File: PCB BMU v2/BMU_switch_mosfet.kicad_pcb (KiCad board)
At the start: 2 copper layers, 18 parts, among them Q1 BC337, Q10 IRF4905STRLPBF, Q2 IRF4905STRLPBF, Q3 IRF4905STRLPBF, Q4 IRF4905STRLPBF, Q5 IRF4905STRLPBF, Q6 BC337, Q7 IRF4905STRLPBF, Q8 IRF4905STRLPBF, Q9 IRF4905STRLPBF, U1 HX PZ2.54-1X2P ZZ, U2 ZX-IDC2.54-2-5PZZ, U3 ZX-IDC2.54-2-5PZZ

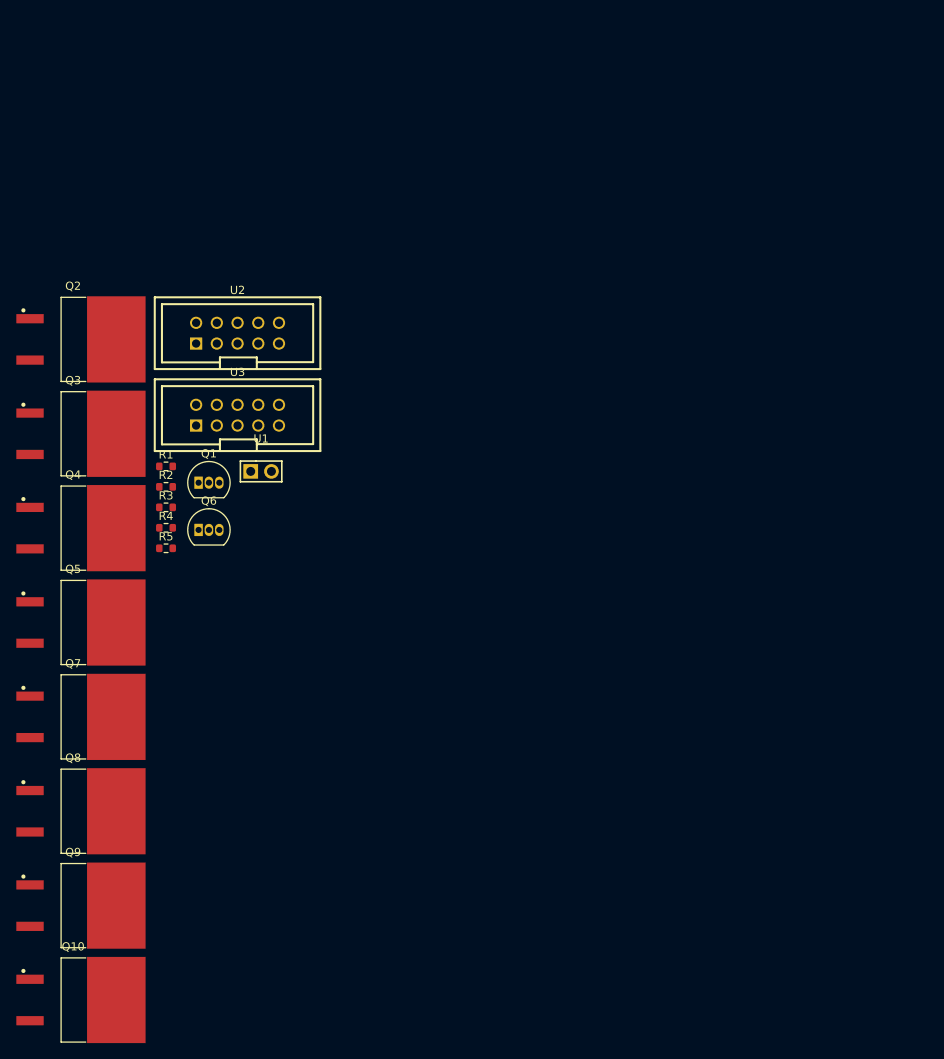
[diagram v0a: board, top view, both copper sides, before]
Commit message: add Ampère/Houre calculation
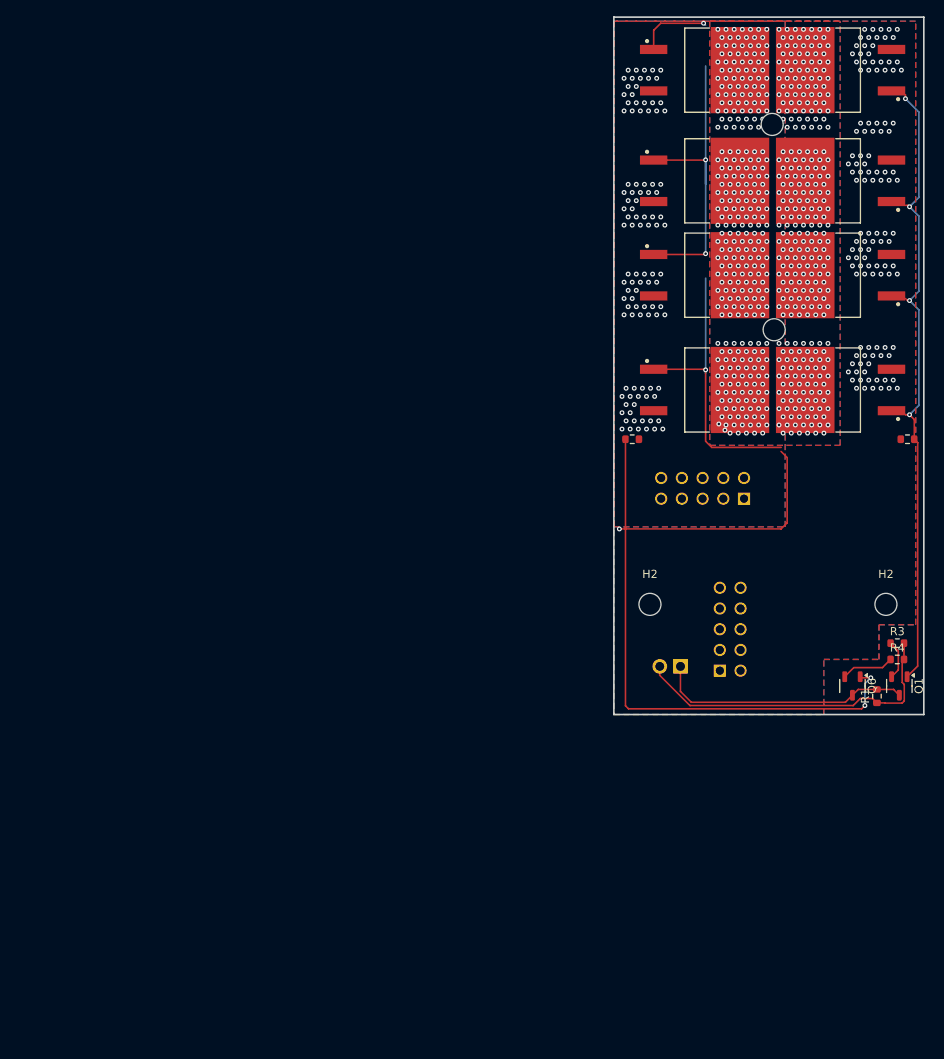
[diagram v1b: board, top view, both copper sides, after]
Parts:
- added H1: MountingHole, MountingHole:MountingHole_2.7mm_M2.5, B.Cu at (144.7, 49.8)
- added H1: MountingHole, MountingHole:MountingHole_2.7mm_M2.5, B.Cu at (144.4, 24.7)
- added H2: MountingHole, MountingHole:MountingHole_2.7mm_M2.5, F.Cu at (129.4, 83.5)
- added H2: MountingHole, MountingHole:MountingHole_2.7mm_M2.5, F.Cu at (158.4, 83.5)
- Q1, Q6: footprint Package_TO_SOT_THT:TO-92_Inline -> Package_TO_SOT_SMD:SOT-23-3
- U1, U2, U3: moved to B.Cu
- moved Q5 116.7 mm to (153.8, 18.0), turned to 180 degrees
- moved Q7 110.2 mm to (135.2, 18.0)
- moved Q9 108.7 mm to (135.2, 43.1)
- moved Q8 108.7 mm to (135.2, 31.6)
- moved Q10 107.0 mm to (135.2, 57.2)
- moved Q4 104.1 mm to (153.8, 31.6), turned to 180 degrees
- moved Q3 97.0 mm to (153.8, 43.1), turned to 180 degrees
- moved Q2 95.2 mm to (153.8, 57.2), turned to 180 degrees
- moved R1 91.6 mm to (157.2, 94.8), turned to 90 degrees
- moved R3 91.2 mm to (159.8, 88.2)
- moved R4 91.1 mm to (159.8, 90.2)
- moved R2 91.1 mm to (161.0, 63.2), turned to 180 degrees
- moved Q1 89.5 mm to (160.0, 93.5), turned to -90 degrees
- moved Q6 82.4 mm to (154.2, 93.5), turned to -90 degrees
- moved U2 70.5 mm to (139.3, 86.5), turned to 90 degrees
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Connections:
- net Net-(Q10-D) renamed /Drain
- net Net-(Q2-S) renamed /+BATT_IN
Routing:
- net Net-(Q10-G): track 0.00 -> 181.3 mm, vias 0 -> 7
- net Net-(Q1-C): track 0.00 -> 77.1 mm, vias 0 -> 4
- net /CMD_Switch_bat: track 0.00 -> 40.5 mm
- net GND: track 0.00 -> 31.4 mm
- net Net-(Q6-B): track 0.00 -> 6.50 mm
- net Net-(Q1-B): track 0.00 -> 4.85 mm
- net /Drain: vias 0 -> 598
- net /+BATT_IN: vias 0 -> 112
- net /+BATT OUT: vias 0 -> 100
- added copper zone on B.Cu, net /+BATT OUT
- added copper zone on F.Cu, net /+BATT OUT
- added copper zone on B.Cu, net /+BATT_IN
- added copper zone on F.Cu, net /+BATT_IN
- added copper zone on B.Cu, net /Drain
- added copper zone on F.Cu, net /Drain
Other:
- board outline added: 38 x 85.5 mm
